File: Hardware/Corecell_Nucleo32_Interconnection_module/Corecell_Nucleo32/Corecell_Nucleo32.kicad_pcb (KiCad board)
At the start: 2 copper layers, 90 x 92 mm, 30 parts, among them IC1 PCI_EXPRESS_CARD, J1 Conn_01x19, J2 Conn_01x19, J3 Bus Standard, J4 Calculatrice_UART_groove, J5 RAK5146_UART_groove(GPS), J6 RAK5146_I2C_groove(GPS), J7 RAK5146_SPI_groove(MCU), Q1 BC548, U1 ESP32-DEVKITC-32D

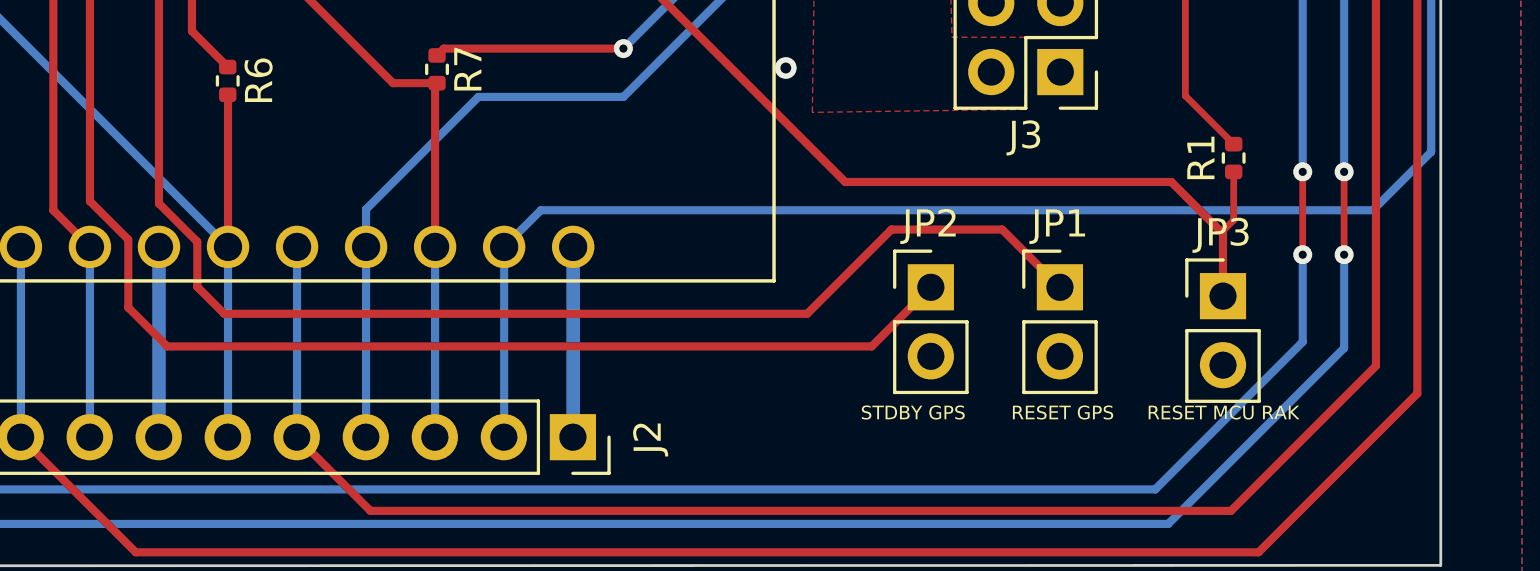
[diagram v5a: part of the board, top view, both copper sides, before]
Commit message: The reset jumpers were changed the footprint for a push button.
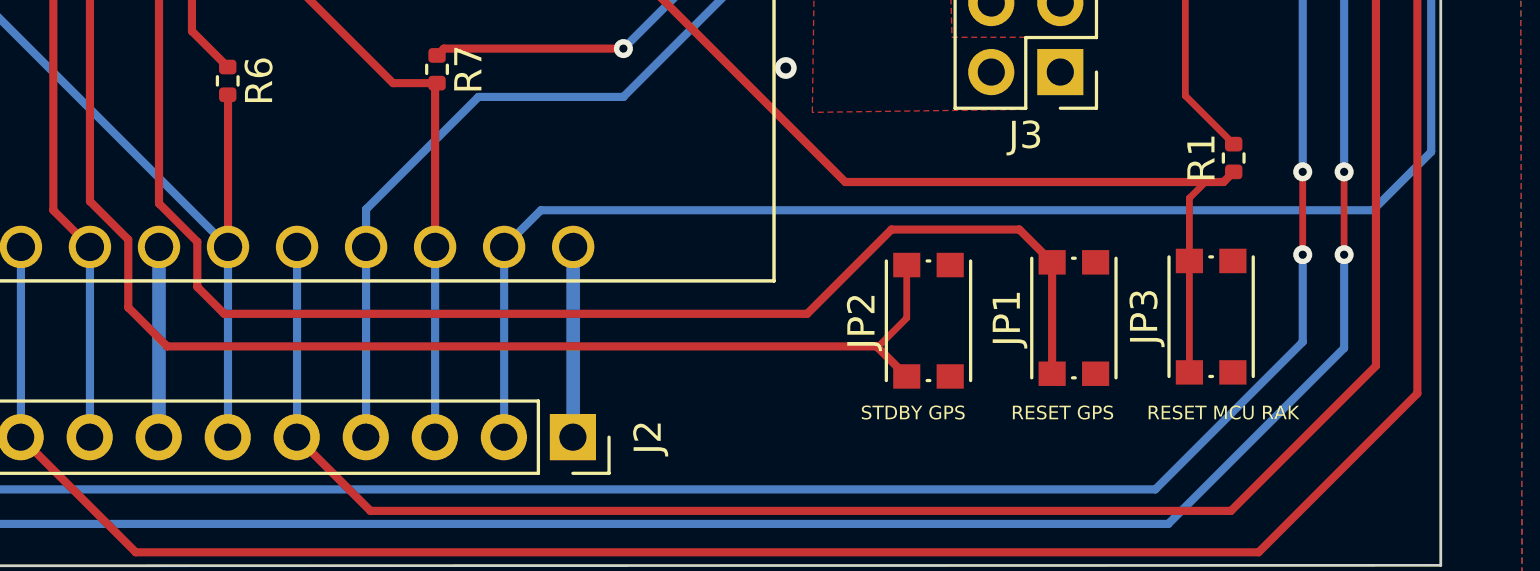
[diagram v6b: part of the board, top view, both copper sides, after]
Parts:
- JP1, JP2, JP3: footprint Connector_PinHeader_2.54mm:PinHeader_1x02_P2.54mm_Vertical -> Button_Switch_SMD:SW_Push_1P1T_NO_CK_KMR2
- moved JP1 1.24 mm to (180.9, 111.0), turned to 90 degrees
- moved JP2 1.23 mm to (175.6, 111.1), turned to 90 degrees
- moved JP3 0.87 mm to (186.0, 111.0), turned to 90 degrees
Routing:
- net /7: track 72.9 -> 76.4 mm
- net /6: track 64.7 -> 67.0 mm
- net /8: track 115.0 -> 117.1 mm
